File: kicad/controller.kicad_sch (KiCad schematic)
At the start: 66 parts, among them U12 SN75176BP, U13 6N137, U3 Pico, U5 L7805, U6 MCP3464R, U7 LF33_TO220, U8 6N137, U9 SN75176BP

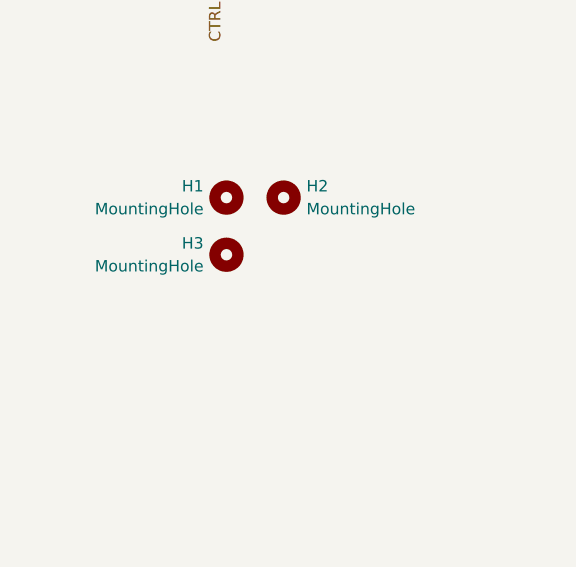
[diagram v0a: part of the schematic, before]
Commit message: Separate boards automatically
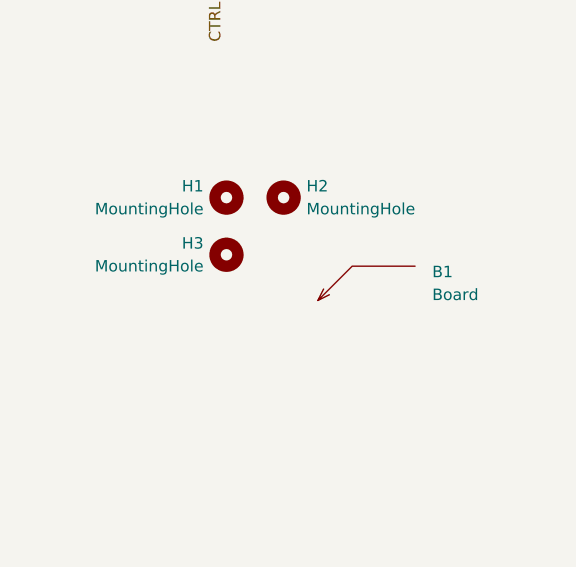
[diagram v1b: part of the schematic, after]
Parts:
- added B1: Board, PCM_kikit:Board, symbol PCM_kikit:Board
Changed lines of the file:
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@@
+    )
+  )
+  (symbol (lib_id "PCM_kikit:Board") (at 250.19 160.02 0) (unit 1)
+    (in_bom no) (on_board yes) (dnp no) (fields_autoplaced)
+    (property "Reference" "B1" (at 262.89 156.845 0)
+      (effects (font (size 1.27 1.27)) (justify left))
+    )
+    (property "Value" "Board" (at 262.89 159.385 0)
+      (effects (font (size 1.27 1.27)) (justify left))
+    )
+    (property "Footprint" "PCM_kikit:Board" (at 260.35 159.385 0)
+      (effects (font (size 1.27 1.27)) hide)
+    )
+    (property "Datasheet" "" (at 250.19 160.02 0)
+      (effects (font (size 1.27 1.27)) hide)
+    )
+    (instances
+      (project "digipsu"
+        (path "/ec5fec7a-fde3-4f44-b689-61159deeeb72/a0108b83-e991-42ef-8684-1d1a6fe91cd6"
+          (reference "B1") (unit 1)
+        )
+      )
     )
   )
